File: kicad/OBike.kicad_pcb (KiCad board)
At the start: 4 copper layers, 60 x 99.2 mm, 73 parts, among them J1 F34G-1A7Q1-E8C40, J2 Micro_SD_Card_Det1, J3 Conn_01x02, J4 Conn_01x04, J5 U.FL-R-SMT-1_10_, J6 Conn_01x02, J7 Conn_01x05, J8 Conn_01x02, Q1 SS8050, Q2 SS8050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

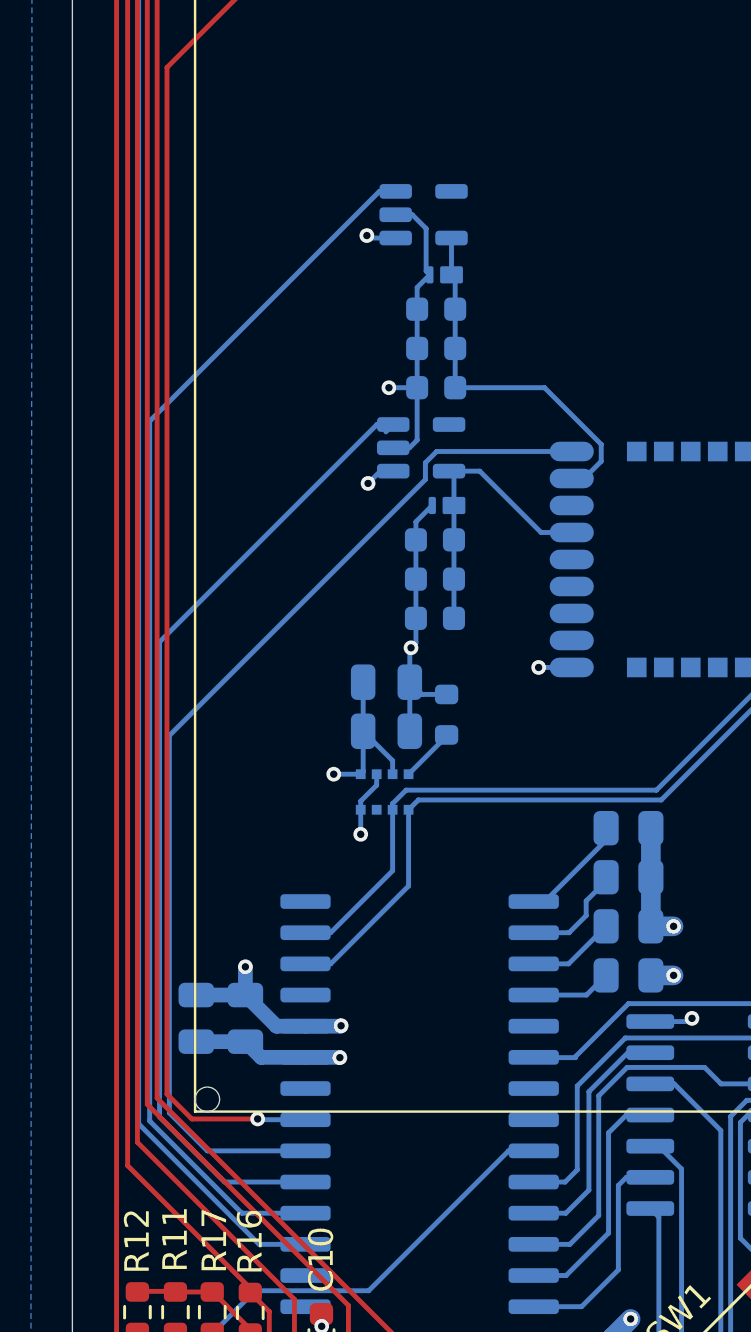
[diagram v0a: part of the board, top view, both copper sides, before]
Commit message: zenners went EOL updated to new device
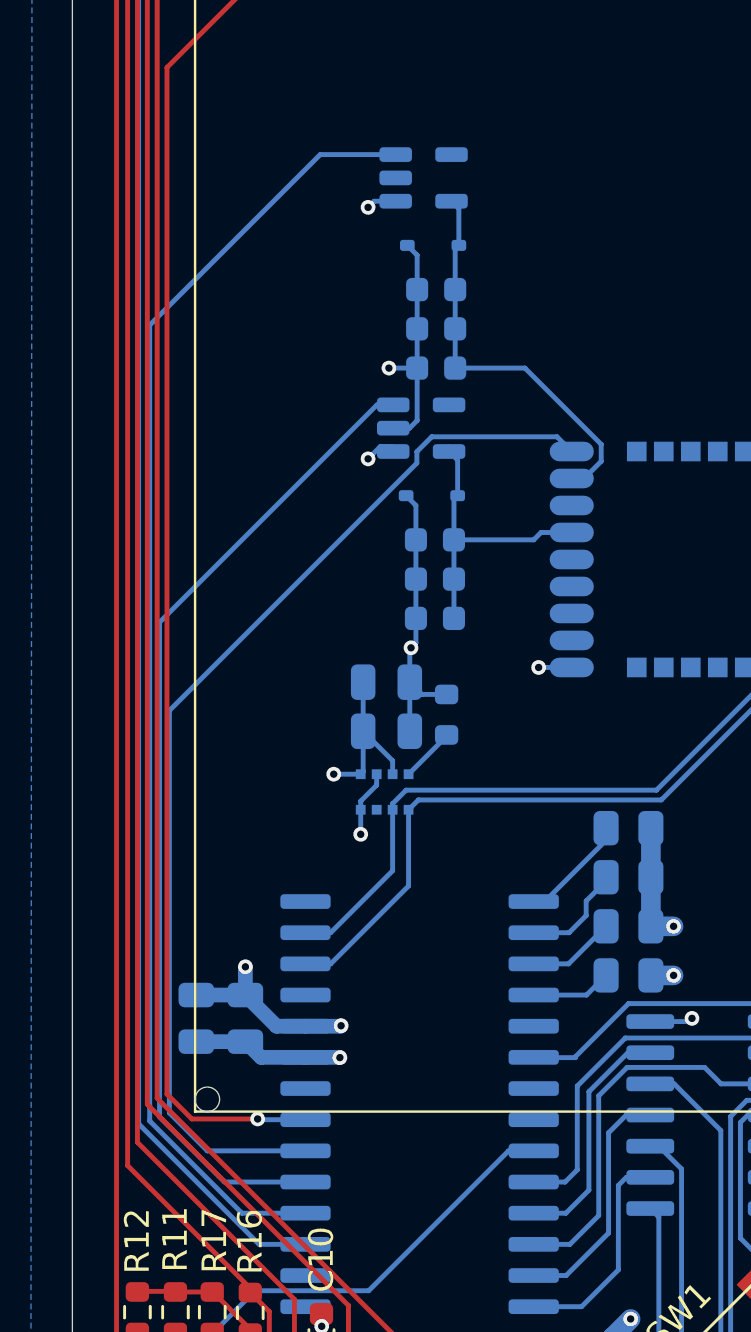
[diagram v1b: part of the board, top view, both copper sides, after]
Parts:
- D6, D7: value PTVS5V0Z1USK -> ESDA051-1JY; footprint Diode_SMD:Nexperia_DSN1608-2_1.6x0.8mm -> Diode_SMD:D_SOD-323
- moved U8 1.50 mm to (132.4, 71.2)
- moved D7 1.29 mm to (132.8, 74.0)
- moved C19 0.80 mm to (132.9, 75.8)
- moved C20 0.80 mm to (132.9, 77.4)
- moved C21 0.80 mm to (132.9, 79.0)
- moved U6 0.80 mm to (132.3, 81.5)
- moved D6 0.73 mm to (132.7, 84.2)
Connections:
- J1 pad 15: SCR_RST -> unconnected-(J1-Pad15)
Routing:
- net GPS_EN: track 50.3 -> 53.2 mm
- net GND: track 99.7 -> 96.9 mm
- net GPS_VCC: track 15.3 -> 16.4 mm
- net GPS_RST: track 43.2 -> 44.1 mm
